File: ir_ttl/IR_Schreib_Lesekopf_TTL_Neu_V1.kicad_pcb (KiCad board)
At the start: 2 copper layers, 18 parts, among them IC1 74LVC1G17DBVR, IC2 74LVC1G17DBVR, T1 SFH309FA-4, T2 BC807-40, T3 BC817-40, X1 +Ub, X2 TXD, X3 RXD, X4 GND

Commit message: updated some footprints and cutouts WIP
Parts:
- D1: moved to B.Cu
- IC1, IC2: footprint IR_Schreib_Lesekopf_TTL_Neu_V1:SOT23_5 -> Package_TO_SOT_SMD:SOT-23-5
- moved IC1 11.5 mm to (146.2, 99.8)
- moved IC2 11.3 mm to (157.2, 103.3), turned to 90 degrees
- turned D1 to 180 degrees
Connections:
- C1 pad 1: +UB -> /VDD
- C2 pad 1: +UB -> /VDD
- C3 pad 1: +UB -> /VDD
- D2 pad 1: +UB -> /VDD
- IC1 pad 1: (no net) -> unconnected-(IC1-NC-Pad1)
- IC1 pad 2: SIG$4 -> Net-(IC1-Pad2)
- IC1 pad 4: 1 -> /VDD
- IC1 pad 5: +UB -> /VDD
- IC2 pad 1: (no net) -> unconnected-(IC2-NC-Pad1)
- IC2 pad 2: OUT -> Net-(IC2-Pad2)
- IC2 pad 4: SIG$5 -> Net-(IC2-Pad4)
- IC2 pad 5: +UB -> /VDD
- R4 pad 2: +UB -> /VDD
- T1 pad 2: +UB -> /VDD
- T2 pad 2: +UB -> /VDD
- X3 pad 1: SIG$5 -> /VDD
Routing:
- net /VDD: track 0.00 -> 41.4 mm
- net GND: track 29.6 -> 0.00 mm
- net +UB: track 28.3 -> 0.00 mm
- net SIG$5: track 13.1 -> 0.00 mm
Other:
- board outline added: 26.9 x 26.9 mm

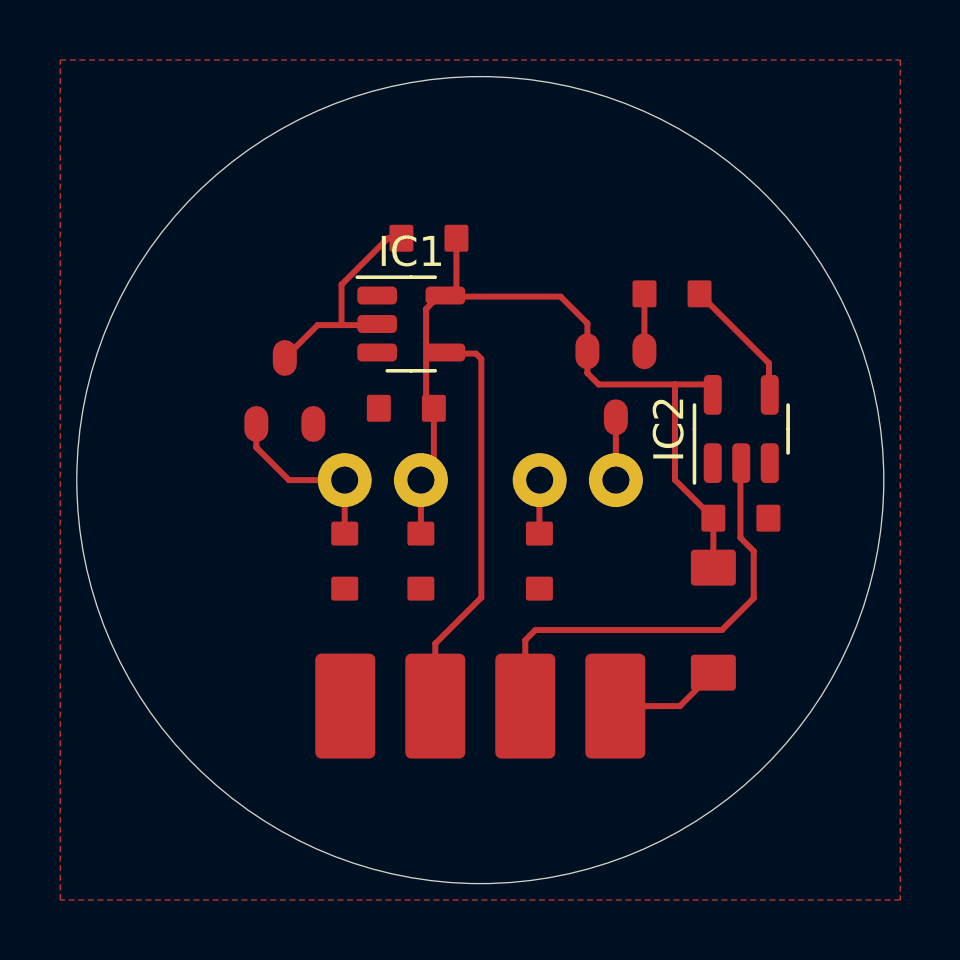
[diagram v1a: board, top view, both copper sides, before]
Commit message: ir_ttl passing DRC
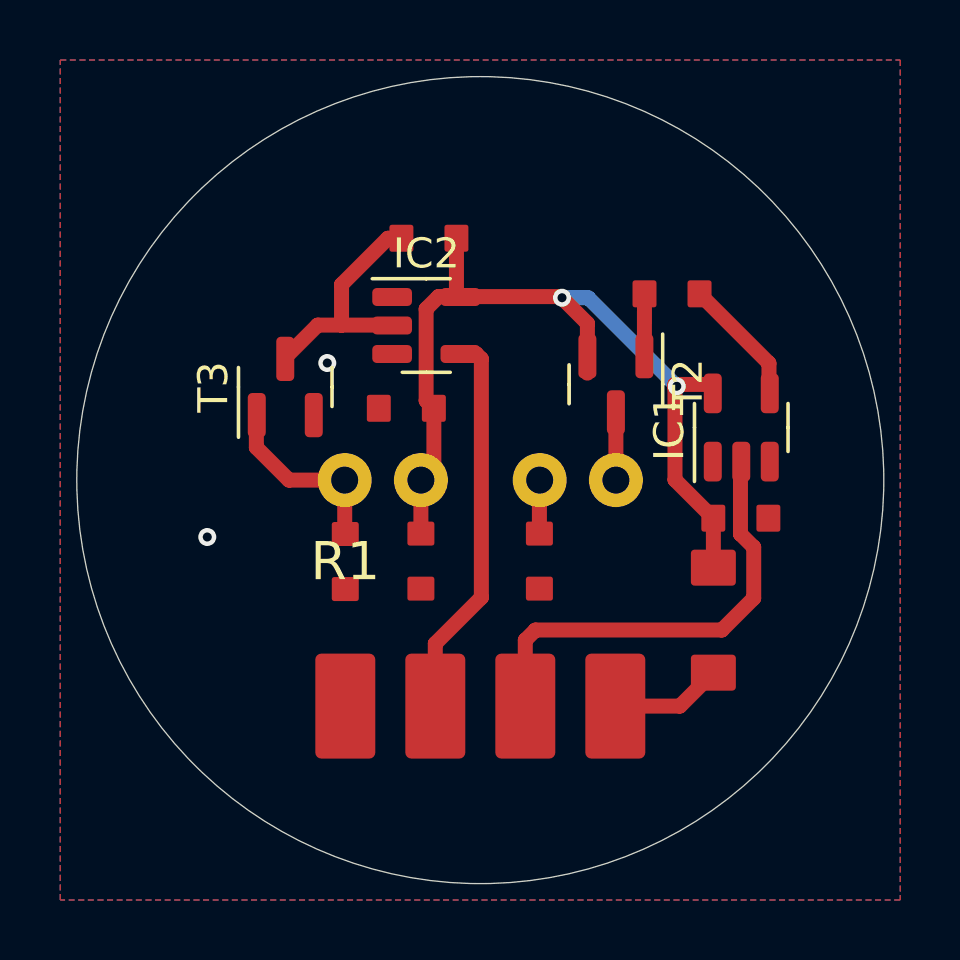
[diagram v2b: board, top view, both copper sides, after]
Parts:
- T2, T3: footprint IR_Schreib_Lesekopf_TTL_Neu_V1:SOT23_3 -> Package_TO_SOT_SMD:SOT-23
- moved IC1 11.5 mm to (157.2, 103.2), turned to 90 degrees
- moved IC2 11.1 mm to (146.7, 99.8), turned to 0 degrees
- moved T3 0.13 mm to (142.0, 101.9), turned to 90 degrees
- turned T2 to -90 degrees
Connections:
- net + renamed Net-(T3-B)
- net A renamed Net-(D2-A)
- net B renamed Net-(T2-B)
- net C renamed Net-(T2-C)
- net K renamed Net-(D1-Pad2)
- IC1 pad 4: /VDD -> Net-(IC1-Pad4)
- IC2 pad 2: Net-(IC2-Pad2) -> Net-(T3-C)
- R3 pad 1: 1 -> Net-(IC1-Pad4)
- R4 pad 1: OUT -> Net-(T3-C)
- T3 pad 3: OUT -> Net-(T3-C)
- X2 pad 1: SIG$4 -> Net-(IC1-Pad2)
- X3 pad 1: /VDD -> Net-(IC2-Pad4)
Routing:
- net Net-(IC1-Pad2): track 0.00 -> 15.1 mm
- net SIG$4: track 15.1 -> 0.00 mm
- net Net-(IC2-Pad4): track 0.00 -> 13.1 mm
- net /VDD: track 41.4 -> 30.3 mm, vias 0 -> 2
- net OUT: track 7.56 -> 0.00 mm
- net Net-(T3-C): track 0.00 -> 7.56 mm
- net Net-(IC1-Pad4): track 0.00 -> 3.98 mm
- net 1: track 3.98 -> 0.00 mm
- net GND: vias 0 -> 2
- added copper zone on B.Cu, net GND
